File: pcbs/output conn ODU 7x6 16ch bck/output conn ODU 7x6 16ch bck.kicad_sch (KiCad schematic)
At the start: 43 parts, among them J1 ODU-MAC_Zero_6x7, J2 Conn_02x25_Odd_Even, J3 Conn_02x25_Odd_Even

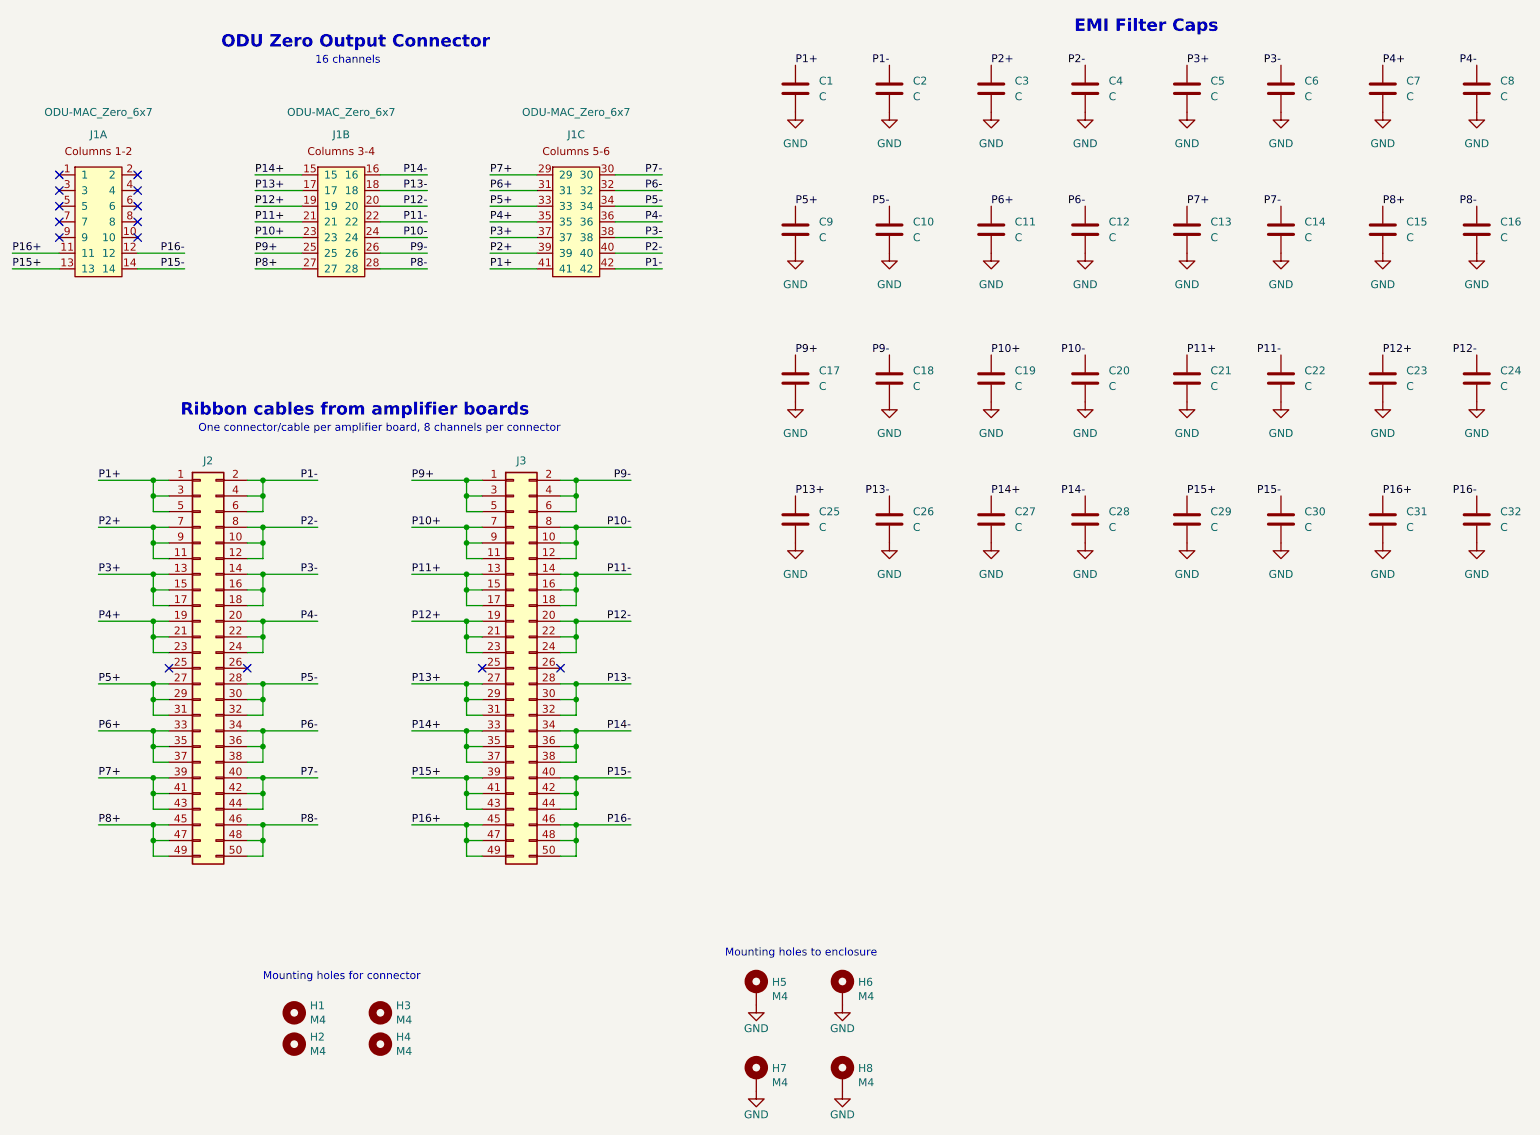
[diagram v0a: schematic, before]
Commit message: Added extra channels to fwd and bck boards
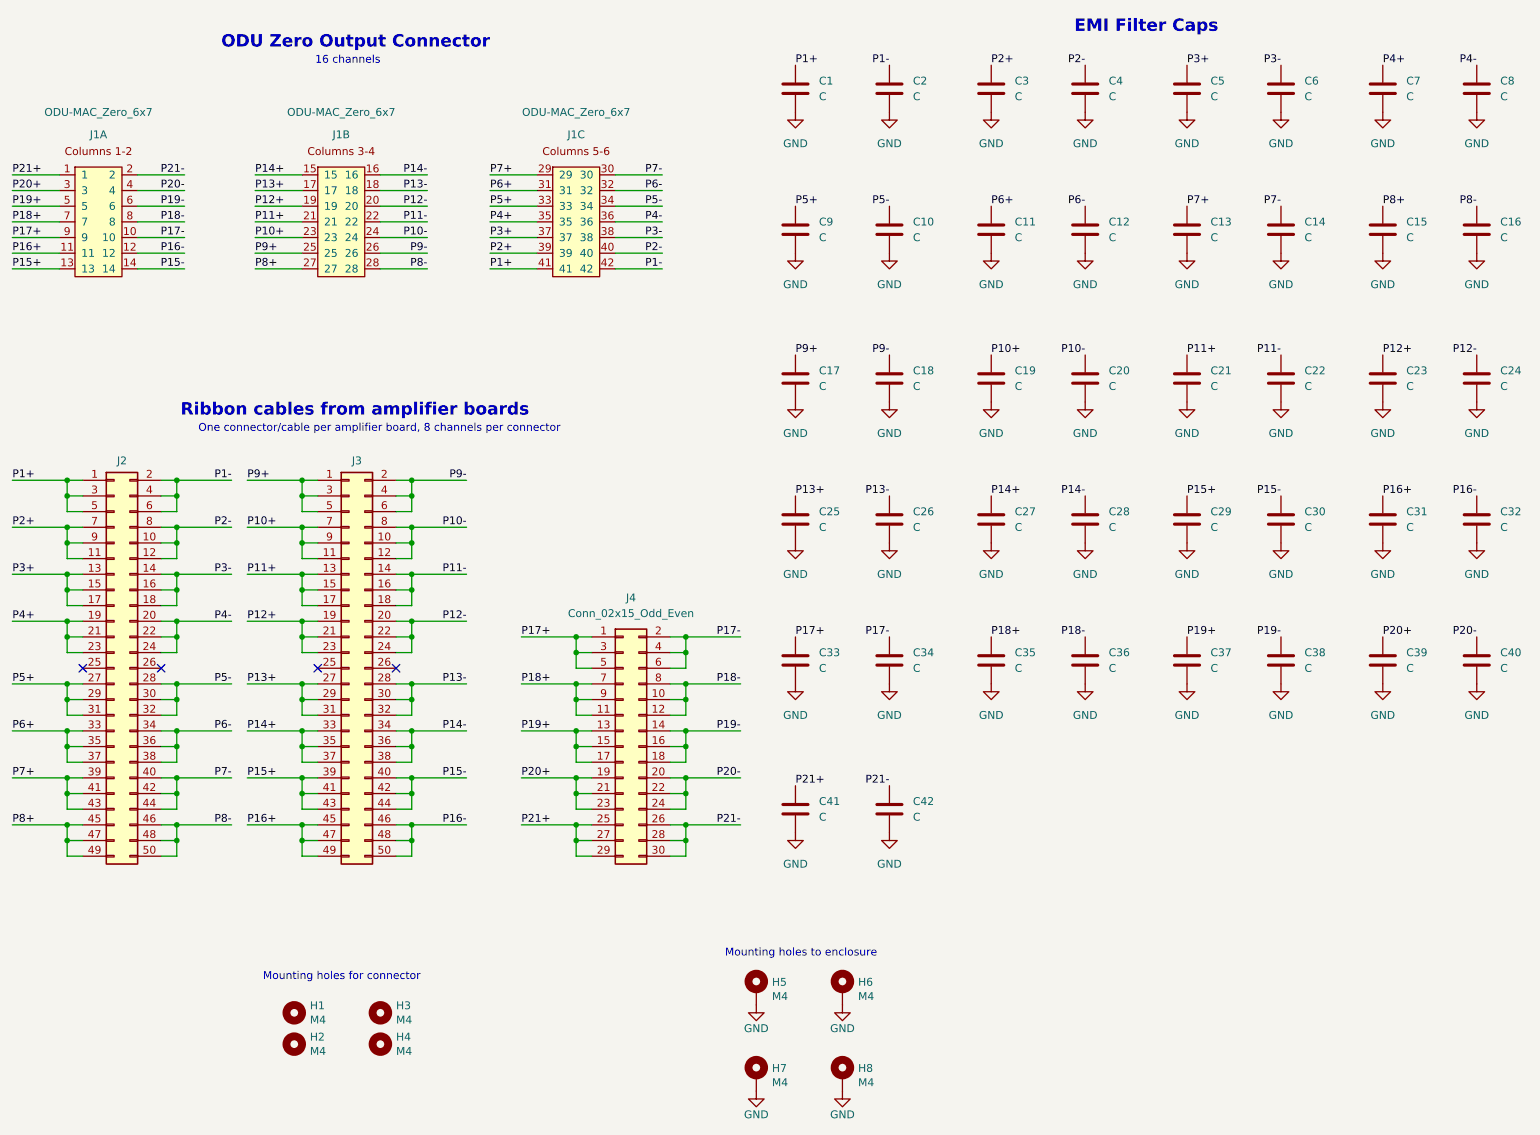
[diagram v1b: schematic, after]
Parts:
- added C33, C34, C35, C36, C37, C38, C39, C40, C41, C42: C, Capacitor_SMD:C_0603_1608Metric, symbol Device:C
- added J4: Conn_02x15_Odd_Even, shim_amp_linear:PinHeader_2x15_P2.54mm_Vertical_Shrouded, symbol Connector_Generic:Conn_02x15_Odd_Even
- J2, J3: footprint Martinos_std:PinHeader_2x25_P2.54mm_Vertical_Shrouded -> shim_amp_linear:PinHeader_2x25_P2.54mm_Vertical_Shrouded
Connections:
- net GND: now also C33.2, C34.2, C35.2, C36.2, C37.2, C38.2, C39.2, C40.2, C41.2, C42.2
- net P21+: now reaches J1.1
- net P21+: now also C41.1, J4.25 (Pin_25), J4.27 (Pin_27), J4.29 (Pin_29)
- net P17-: now reaches J1.10
- net P17-: now also C34.1, J4.2 (Pin_2), J4.4 (Pin_4), J4.6 (Pin_6)
- net P21-: now reaches J1.2
- net P21-: now also C42.1, J4.26 (Pin_26), J4.28 (Pin_28), J4.30 (Pin_30)
- net P20+: now reaches J1.3
- net P20+: now also C39.1, J4.19 (Pin_19), J4.21 (Pin_21), J4.23 (Pin_23)
- net P20-: now reaches J1.4
- net P20-: now also C40.1, J4.20 (Pin_20), J4.22 (Pin_22), J4.24 (Pin_24)
- net P19+: now reaches J1.5
- net P19+: now also C37.1, J4.13 (Pin_13), J4.15 (Pin_15), J4.17 (Pin_17)
- net P19-: now reaches J1.6
- net P19-: now also C38.1, J4.14 (Pin_14), J4.16 (Pin_16), J4.18 (Pin_18)
- net P18+: now reaches J1.7
- net P18+: now also C35.1, J4.11 (Pin_11), J4.7 (Pin_7), J4.9 (Pin_9)
- net P18-: now reaches J1.8
- net P18-: now also C36.1, J4.10 (Pin_10), J4.12 (Pin_12), J4.8 (Pin_8)
- net P17+: now reaches J1.9
- net P17+: now also C33.1, J4.1 (Pin_1), J4.3 (Pin_3), J4.5 (Pin_5)
- no-connect marks 14 -> 4
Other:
- moved on the sheet: J2, J3

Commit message: Added ODU footprints
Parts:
- J1: footprint Don:ODU-MAC_Zero_6x7 -> shim_amp_linear:ODU-MAC_Zero_6x7_bck
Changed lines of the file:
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@@
 			)
 		)
-		(property "Footprint" "Don:ODU-MAC_Zero_6x7"
+		(property "Footprint" "shim_amp_linear:ODU-MAC_Zero_6x7_bck"
 			(at 29.21 53.34 0)
 			(effects
@@
 			)
 		)
-		(property "Footprint" "Don:ODU-MAC_Zero_6x7"
+		(property "Footprint" "shim_amp_linear:ODU-MAC_Zero_6x7_bck"
 			(at 68.58 53.34 0)
 			(effects
@@
 			)
 		)
-		(property "Footprint" "Don:ODU-MAC_Zero_6x7"
+		(property "Footprint" "shim_amp_linear:ODU-MAC_Zero_6x7_bck"
 			(at 106.68 53.34 0)
 			(effects
